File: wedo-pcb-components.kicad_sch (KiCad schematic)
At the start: 6 parts, among them J1 6P6C, J2 6P6C, J3 Conn_01x03_Pin, SW2 SW_Push_Dual_x2, U1 TPS61032

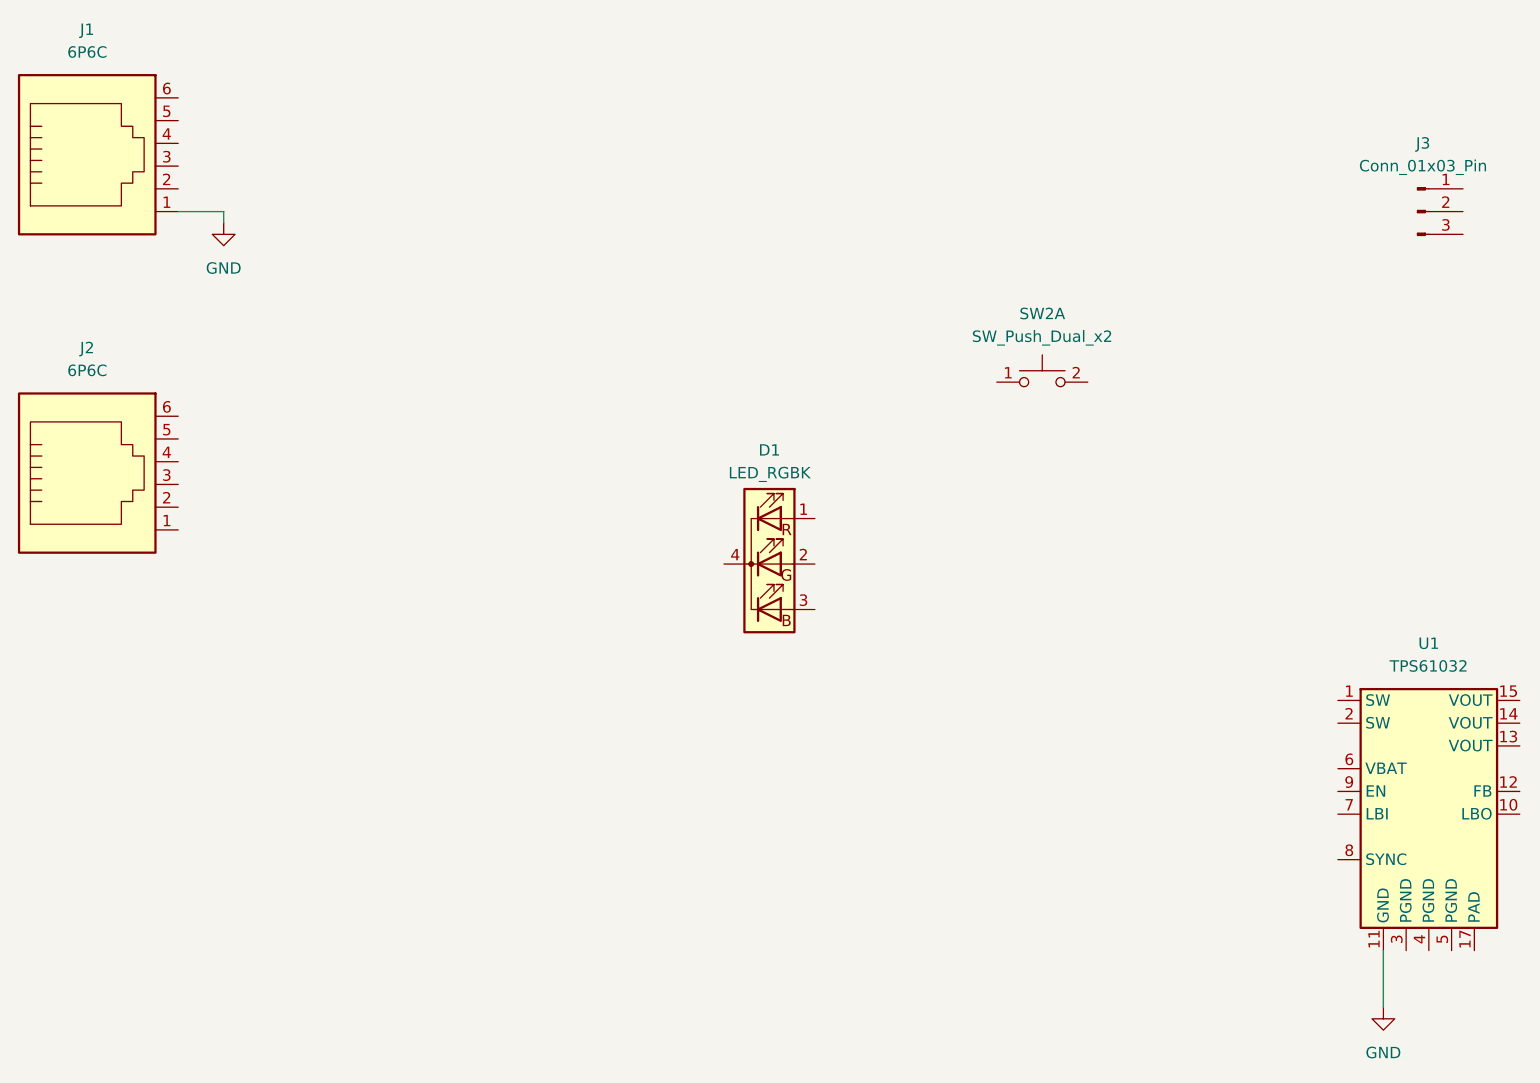
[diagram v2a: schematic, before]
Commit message: Moved motor/sensor connectors further to edges in Y direction (were too close to center by mistake), updated battery blade connector with two holes to also support THD version, slightly moved battery blade connector towards center in X direction for better clearance
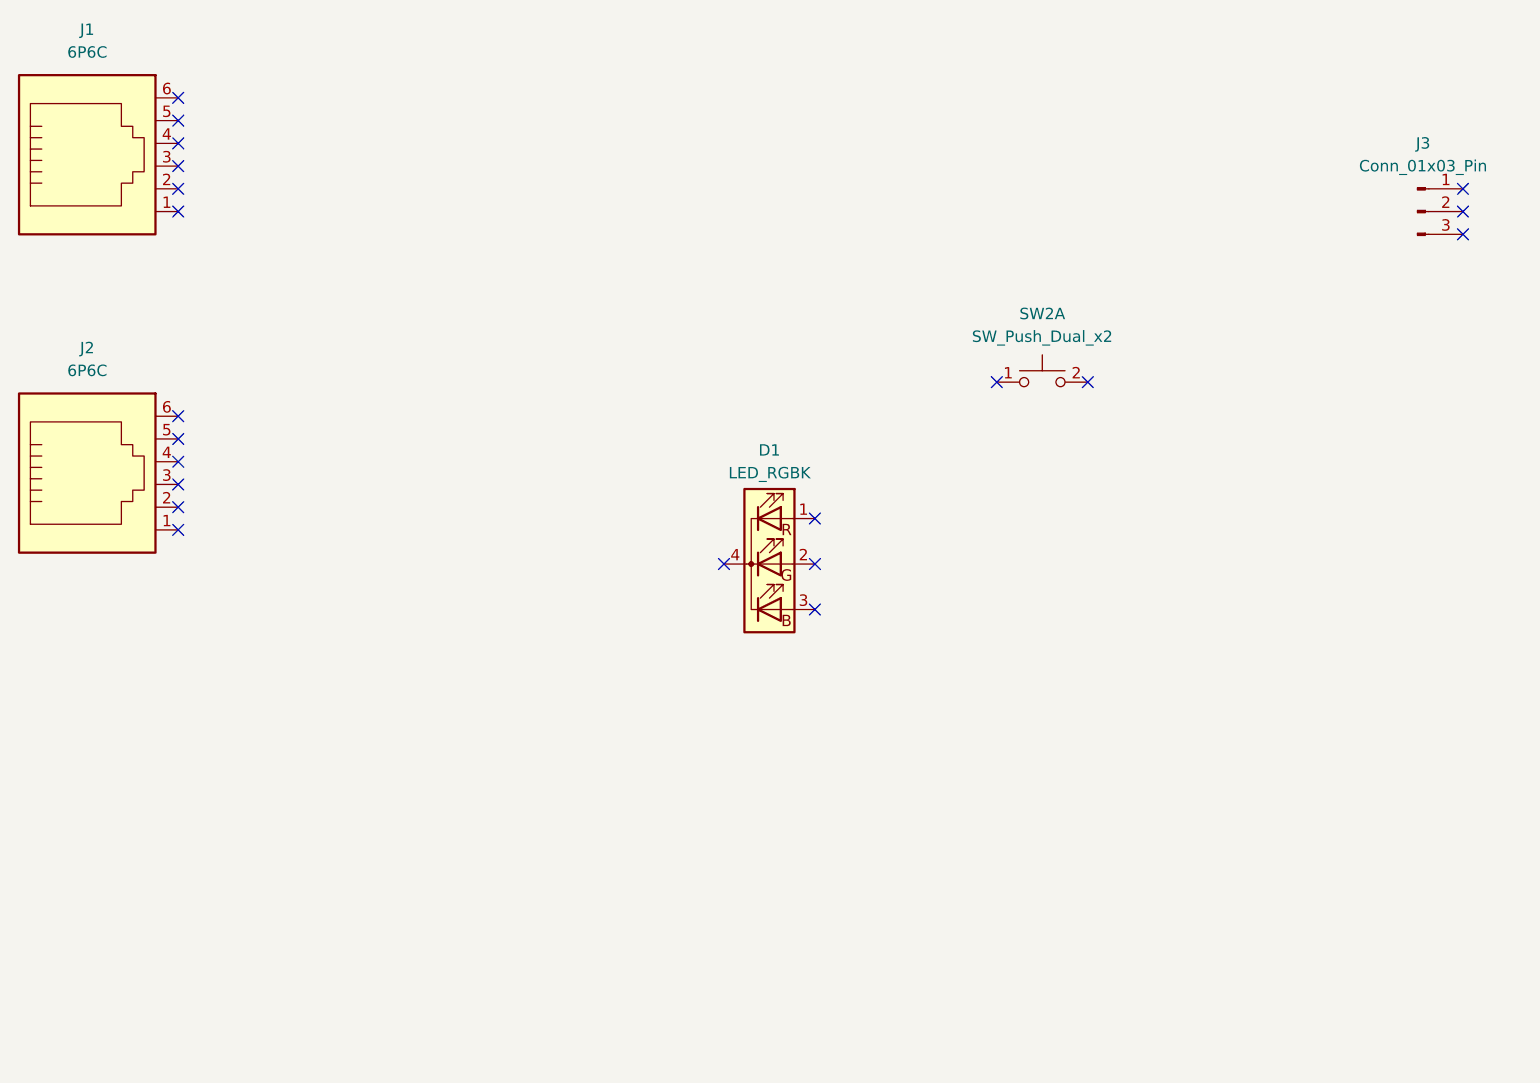
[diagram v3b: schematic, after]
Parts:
- removed U1: TPS61032, Package_SO:HTSSOP-16-1EP_4.4x5mm_P0.65mm_EP3.4x5mm, symbol Regulator_Switching_Boost:TPS61032
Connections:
- net GND: no longer names the net of J1.1
- no-connect marks 0 -> 21
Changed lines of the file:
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@@
 (kicad_sch (version 20230121) (generator eeschema)
   (paper "A4")
-  (wire (pts (xy 203.2 147.32) (xy 203.2 153.67))
-    (stroke (width 0) (type default))
-  )
-  (wire (pts (xy 73.66 64.77) (xy 73.66 66.04))
-    (stroke (width 0) (type default))
-  )
-  (wire (pts (xy 68.58 64.77) (xy 73.66 64.77))
-    (stroke (width 0) (type default))
-  )
+  (no_connect (at 212.09 62.23))
+  (no_connect (at 129.54 104.14))
+  (no_connect (at 68.58 97.79))
+  (no_connect (at 68.58 62.23))
+  (no_connect (at 68.58 59.69))
+  (no_connect (at 139.7 109.22))
+  (no_connect (at 68.58 54.61))
+  (no_connect (at 68.58 90.17))
+  (no_connect (at 68.58 57.15))
+  (no_connect (at 212.09 67.31))
+  (no_connect (at 139.7 104.14))
+  (no_connect (at 68.58 64.77))
+  (no_connect (at 139.7 99.06))
+  (no_connect (at 68.58 100.33))
+  (no_connect (at 68.58 52.07))
+  (no_connect (at 160.02 83.82))
+  (no_connect (at 170.18 83.82))
+  (no_connect (at 68.58 87.63))
+  (no_connect (at 212.09 64.77))
+  (no_connect (at 68.58 92.71))
+  (no_connect (at 68.58 95.25))
   (symbol (lib_id "Connector:Conn_01x03_Pin") (at 207.01 64.77 0) (unit 1)
     (in_bom yes) (on_board yes) (dnp no) (fields_autoplaced)
@@
         (path "/3b24d53b-e226-431a-952a-6b8641a91fb3"
           (reference "J3") (unit 1)
-        )
-      )
-    )
-  )
-  (symbol (lib_id "Regulator_Switching_Boost:TPS61032") (at 208.28 132.08 0) (unit 1)
-    (in_bom yes) (on_board yes) (dnp no) (fields_autoplaced)
-    (property "Reference" "U1" (at 208.28 113.03 0)
-      (effects (font (size 1.27 1.27)))
-    )
-    (property "Value" "TPS61032" (at 208.28 115.57 0)
-      (effects (font (size 1.27 1.27)))
-    )
-    (property "Footprint" "Package_SO:HTSSOP-16-1EP_4.4x5mm_P0.65mm_EP3.4x5mm" (at 184.15 158.75 0)
-      (effects (font (size 1.27 1.27)) (justify left) hide)
-    )
-    (property "Datasheet" "https://www.ti.com/lit/ds/symlink/tps61032.pdf" (at 212.09 161.29 0)
-      (effects (font (size 1.27 1.27)) (justify left) hide)
-    )
-    (pin "9")
-    (pin "7")
-    (pin "17")
-    (pin "8")
-    (pin "5")
-    (pin "13")
-    (pin "14")
-    (pin "1")
-    (pin "4")
-    (pin "3")
-    (pin "2")
-    (pin "12")
-    (pin "11")
-    (pin "10")
-    (pin "16")
-    (pin "15")
-    (pin "6")
-    (instances
-      (project "wedo-pcb-components"
-        (path "/3b24d53b-e226-431a-952a-6b8641a91fb3"
-          (reference "U1") (unit 1)
         )
       )
@@
         )
       )
-    )
-  )
-  (symbol (lib_id "power:GND") (at 203.2 153.67 0) (unit 1)
-    (in_bom yes) (on_board yes) (dnp no) (fields_autoplaced)
-    (property "Reference" "#PWR01" (at 203.2 160.02 0)
-      (effects (font (size 1.27 1.27)) hide)
-    )
-    (property "Value" "GND" (at 203.2 158.75 0)
-      (effects (font (size 1.27 1.27)))
-    )
-    (property "Footprint" "" (at 203.2 153.67 0)
-      (effects (font (size 1.27 1.27)) hide)
-    )
-    (property "Datasheet" "" (at 203.2 153.67 0)
-      (effects (font (size 1.27 1.27)) hide)
-    )
-    (pin "1")
-    (instances
-      (project "wedo-pcb-components"
-        (path "/3b24d53b-e226-431a-952a-6b8641a91fb3"
-          (reference "#PWR01") (unit 1)
-        )
-      )
-    )
-  )
-  (symbol (lib_id "power:GND") (at 73.66 66.04 0) (unit 1)
-    (in_bom yes) (on_board yes) (dnp no) (fields_autoplaced)
-    (property "Reference" "#PWR02" (at 73.66 72.39 0)
-      (effects (font (size 1.27 1.27)) hide)
-    )
-    (property "Value" "GND" (at 73.66 71.12 0)
-      (effects (font (size 1.27 1.27)))
-    )
-    (property "Footprint" "" (at 73.66 66.04 0)
-      (effects (font (size 1.27 1.27)) hide)
-    )
-    (property "Datasheet" "" (at 73.66 66.04 0)
-      (effects (font (size 1.27 1.27)) hide)
-    )
-    (pin "1")
-    (instances
-      (project "wedo-pcb-components"
-        (path "/3b24d53b-e226-431a-952a-6b8641a91fb3"
-          (reference "#PWR02") (unit 1)
-        )
-      )
